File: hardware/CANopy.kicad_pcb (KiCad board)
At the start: 2 copper layers, 65 x 56.5 mm, 42 parts, among them J1 RPi_GPIO, J2 CAN0, J3 CAN1, J4 CAN2, U1 MCP2518FD-xQBB, U2 MCP2562FD-E/SN, U3 MCP2518FD-xQBB, U4 MCP2562FD-E/SN, U5 MCP2518FD-xQBB, U6 MCP2562FD-E/SN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

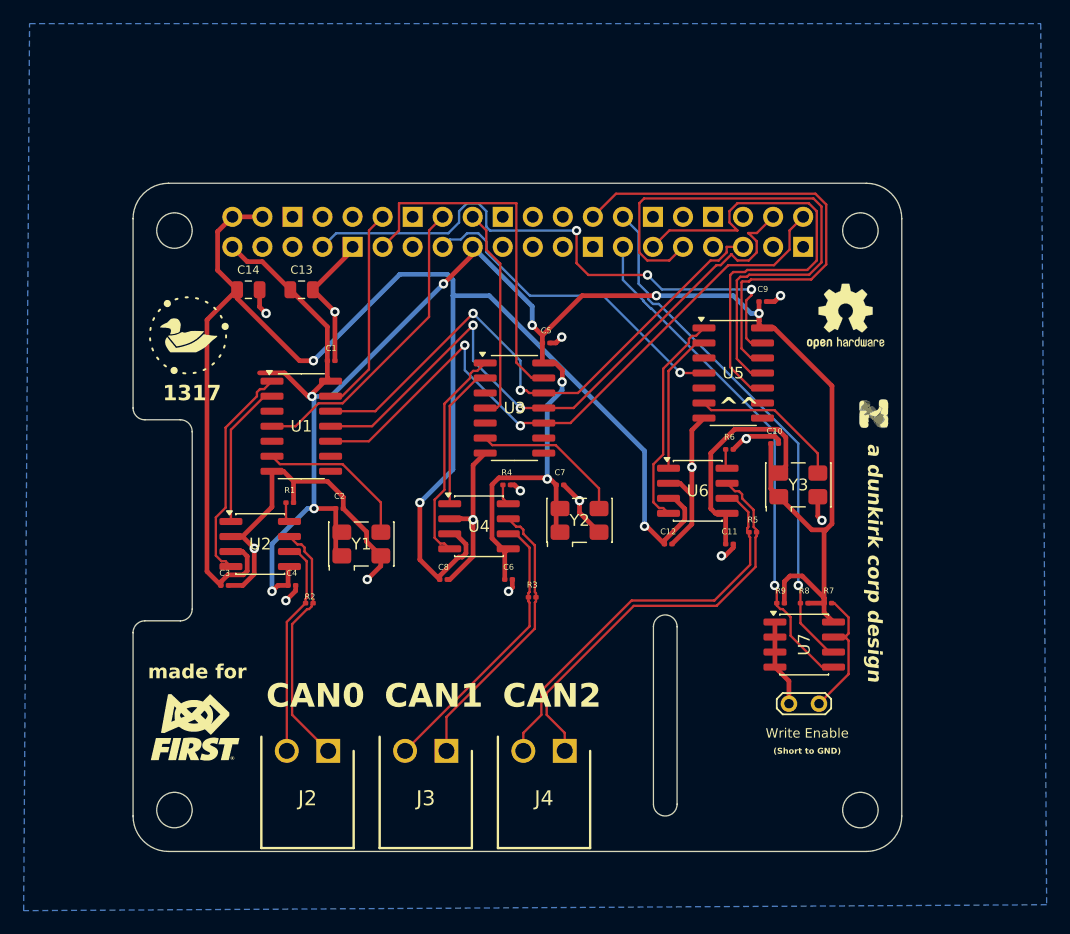
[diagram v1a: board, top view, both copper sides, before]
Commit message: feat: update schematic with proper cap sizes
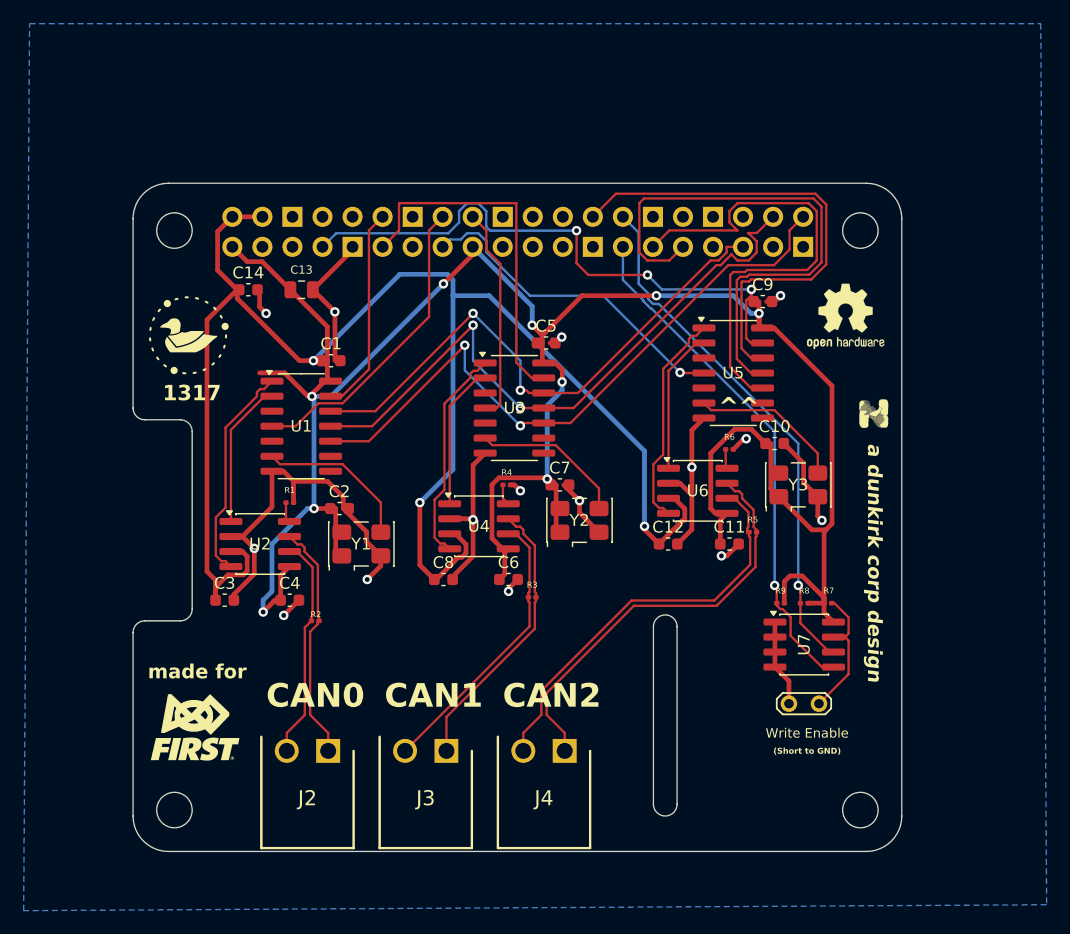
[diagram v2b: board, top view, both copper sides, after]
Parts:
- C1, C10, C11, C12, C2, C3, C4, C5, C6, C7, C8, C9: value 100nF -> 1µF; footprint Capacitor_SMD:C_0201_0603Metric -> Capacitor_SMD:C_0603_1608Metric
- C14: value 10µF -> 1µF; footprint Capacitor_SMD:C_0805_2012Metric -> Capacitor_SMD:C_0603_1608Metric
- moved R2 1.58 mm to (56.7, 73.5)
- moved C4 1.26 mm to (54.5, 71.8)
- moved C3 1.25 mm to (49.0, 71.8)
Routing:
- net GND: track 102.2 -> 105.3 mm
- net +5V: track 135.3 -> 138.0 mm
- net /CAN0/CAN_P: track 21.2 -> 20.3 mm
- net +3.3V: track 202.3 -> 201.8 mm

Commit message: feat: first pass reroute
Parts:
- C14: value 1µF -> 10µF; footprint Capacitor_SMD:C_0603_1608Metric -> Capacitor_SMD:C_0805_2012Metric
- J2, J3, J4: footprint Degson:SHDRRA2W80P0X350_1X2_780X920X722P -> Degson:CONN-TH_DG500-5.08-02P-14-00A-H
- R1, R2, R3, R4, R5, R6, R7, R8, R9: footprint Resistor_SMD:R_0201_0603Metric -> Resistor_SMD:R_0603_1608Metric
- moved C2 25.3 mm to (80.0, 50.2)
- moved C6 23.6 mm to (50.0, 64.8)
- moved Y2 22.2 mm to (59.0, 55.2), turned to 180 degrees
- moved Y1 22.0 mm to (78.2, 54.0), turned to 180 degrees
- moved C5 16.0 mm to (82.3, 64.8)
- moved C8 11.2 mm to (77.5, 65.0), turned to 180 degrees
- moved R6 11.1 mm to (102.5, 56.5)
- moved R4 10.9 mm to (82.5, 57.0)
- moved C3 10.8 mm to (58.3, 66.2), turned to 180 degrees
- moved R3 10.3 mm to (84.6, 67.8)
- moved C4 10.1 mm to (63.0, 66.2)
- moved R1 10.1 mm to (63.3, 58.5)
- moved C12 9.78 mm to (96.1, 65.0), turned to 180 degrees
- moved U4 9.74 mm to (79.0, 60.8)
- moved R2 9.72 mm to (65.3, 69.0)
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- renumbered G*** to duck-logo, G*** to first-logo, REF** to osh-hw
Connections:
- net /CAN0/XCAN_N renamed Net-(TP2-TX)
- net /CAN0/XCAN_P renamed Net-(TP2-RX)
- net /CAN1/XCAN_N renamed Net-(TP3-TX)
- net /CAN1/XCAN_P renamed Net-(TP3-RX)
- net /CAN2/XCAN_N renamed Net-(TP4-TX)
- net /CAN2/XCAN_P renamed Net-(TP4-RX)
- net /CAN2/XO_OUT renamed Net-(U5-OSC1)
- J2 pad 1: /CAN0/CAN_P -> /CAN0/CAN_N
- J2 pad 2: /CAN0/CAN_N -> /CAN0/CAN_P
- J3 pad 1: /CAN1/CAN_P -> /CAN1/CAN_N
- J3 pad 2: /CAN1/CAN_N -> /CAN1/CAN_P
- J4 pad 1: /CAN2/CAN_P -> /CAN2/CAN_N
- J4 pad 2: /CAN2/CAN_N -> /CAN2/CAN_P
- U1 pad 6: /CAN0/XO_OUT -> Net-(U1-OSC1)
- U3 pad 10: /SPI1_SCLK -> /SPI1_MOSI
- U3 pad 11: /SPI1_MOSI -> /SPI1_SCLK
- U3 pad 6: /CAN1/XO_OUT -> Net-(U3-OSC1)
- U5 pad 10: /SPI3_SCLK -> /SPI3_MOSI
- U5 pad 11: /SPI3_MOSI -> /SPI3_SCLK
- Y1 pad 2: GND -> unconnected-(Y1-GND-Pad2)
- Y1 pad 3: /CAN0/XO_OUT -> Net-(U3-OSC1)
- Y2 pad 2: GND -> unconnected-(Y2-GND-Pad2)
- Y2 pad 3: /CAN1/XO_OUT -> Net-(U1-OSC1)
- Y3 pad 2: GND -> unconnected-(Y3-GND-Pad2)
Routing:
- net +3.3V: track 201.8 -> 9.89 mm, vias 9 -> 2
- net /CAN2/CAN_P: track 35.9 -> 88.9 mm
- net +5V: track 138.0 -> 87.6 mm, vias 3 -> 4
- net /SPI3_CE0: track 49.6 -> 0.00 mm, vias 3 -> 0
- net /CAN2/CAN_N: track 34.6 -> 81.1 mm
- net /SPI3_MOSI: track 46.3 -> 0.00 mm
- net /CAN1/CAN_P: track 23.9 -> 67.5 mm
- net /SPI3_MISO: track 41.5 -> 0.00 mm
- net /SPI3_SCLK: track 40.8 -> 0.00 mm
- net /SPI1_CE1: track 30.5 -> 0.00 mm
- net /SPI3_INT0: track 28.0 -> 0.00 mm, vias 1 -> 0
- net /SPI1_INT0: track 26.0 -> 0.00 mm
- net /CAN1/CAN_N: track 23.9 -> 47.1 mm
- net GND: track 105.3 -> 86.0 mm, vias 15 -> 17
- net /SPI1_MOSI: track 54.7 -> 36.4 mm, vias 2 -> 0
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- added copper zone on F.Cu, net +3.3V
- added copper zone on F.Cu, net +5V
- added copper zone on F.Cu, net GND
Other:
- board text added: "GRN YLW"
- board text removed: "1317"
- board text removed: "U1"
- board text removed: "U3"
- board text removed: "U5"
- board text removed: "^^"

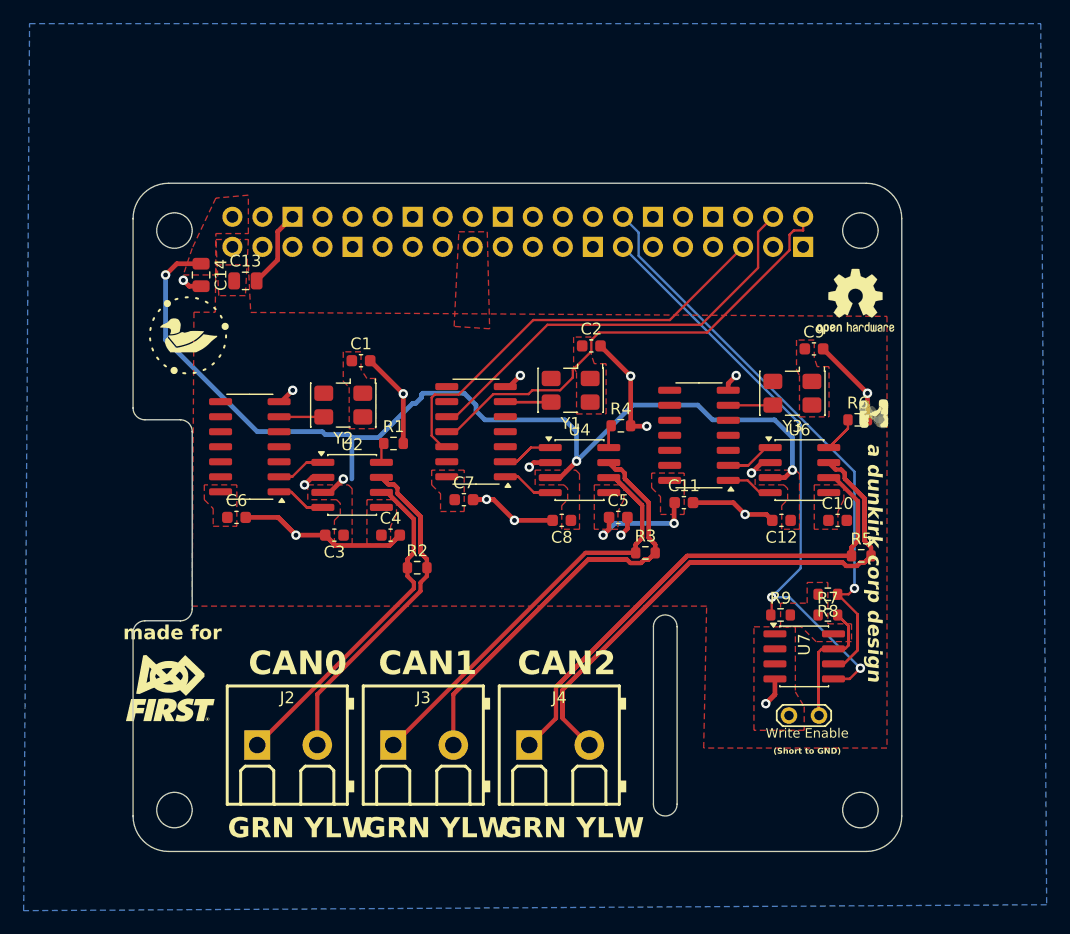
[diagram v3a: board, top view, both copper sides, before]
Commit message: feat: route 4 layer
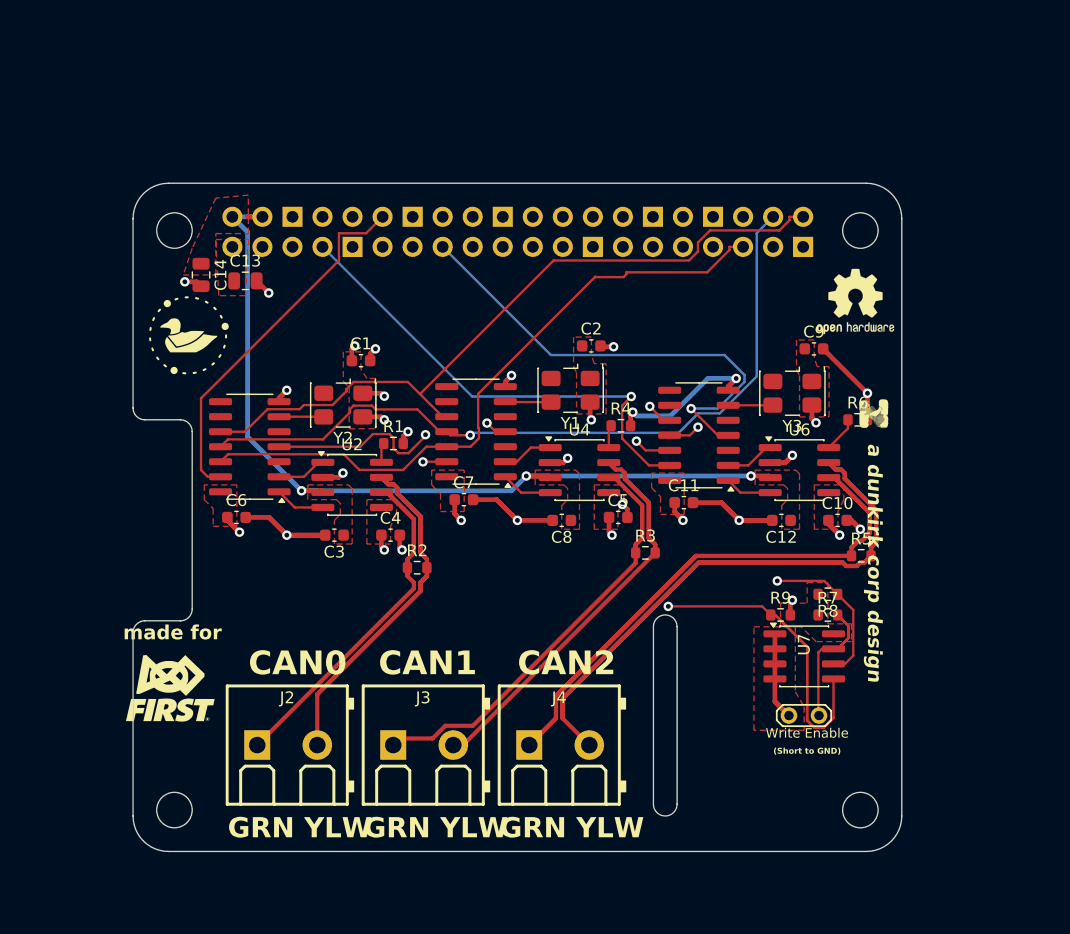
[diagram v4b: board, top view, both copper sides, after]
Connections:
- U3 pad 10: /SPI1_MOSI -> /SPI1_SCLK
- U3 pad 11: /SPI1_SCLK -> /SPI1_MOSI
- U5 pad 10: /SPI3_MOSI -> /SPI3_SCLK
- U5 pad 11: /SPI3_SCLK -> /SPI3_MOSI
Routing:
- net /SPI3_CE0: track 0.00 -> 40.2 mm, vias 0 -> 1
- net /SPI3_INT0: track 0.00 -> 40.1 mm, vias 0 -> 1
- net /SPI1_INT0: track 0.00 -> 33.9 mm, vias 0 -> 1
- net /SPI1_CE0: track 0.00 -> 31.0 mm
- net /ID_SD: track 52.4 -> 81.7 mm, vias 2 -> 1
- net /SPI1_MOSI: track 36.4 -> 64.1 mm, vias 0 -> 1
- net /CAN1/CAN_P: track 67.5 -> 42.4 mm
- net /SPI3_MISO: track 0.00 -> 24.1 mm, vias 0 -> 1
- net /SPI1_CE1: track 0.00 -> 21.6 mm, vias 0 -> 1
- net /SPI1_SCLK: track 40.0 -> 61.4 mm
- net /SPI1_INT1: track 0.00 -> 20.0 mm, vias 0 -> 1
- net /SPI1_MISO: track 36.5 -> 55.4 mm
- net /SPI3_MOSI: track 0.00 -> 18.5 mm, vias 0 -> 1
- net +3.3V: track 9.89 -> 25.8 mm, vias 2 -> 12
- net /SPI3_SCLK: track 0.00 -> 15.8 mm, vias 0 -> 1
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- added copper zone on In2.Cu, net +3.3V
- added copper zone on In1.Cu, net GND
- removed copper zone on B.Cu, net GND
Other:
- copper layers 2 -> 4
